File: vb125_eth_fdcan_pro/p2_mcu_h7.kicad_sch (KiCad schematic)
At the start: 14 parts, among them J1 TAGconnect NL, M1 DM-OLED042-647, U1 STM32H725IGKx

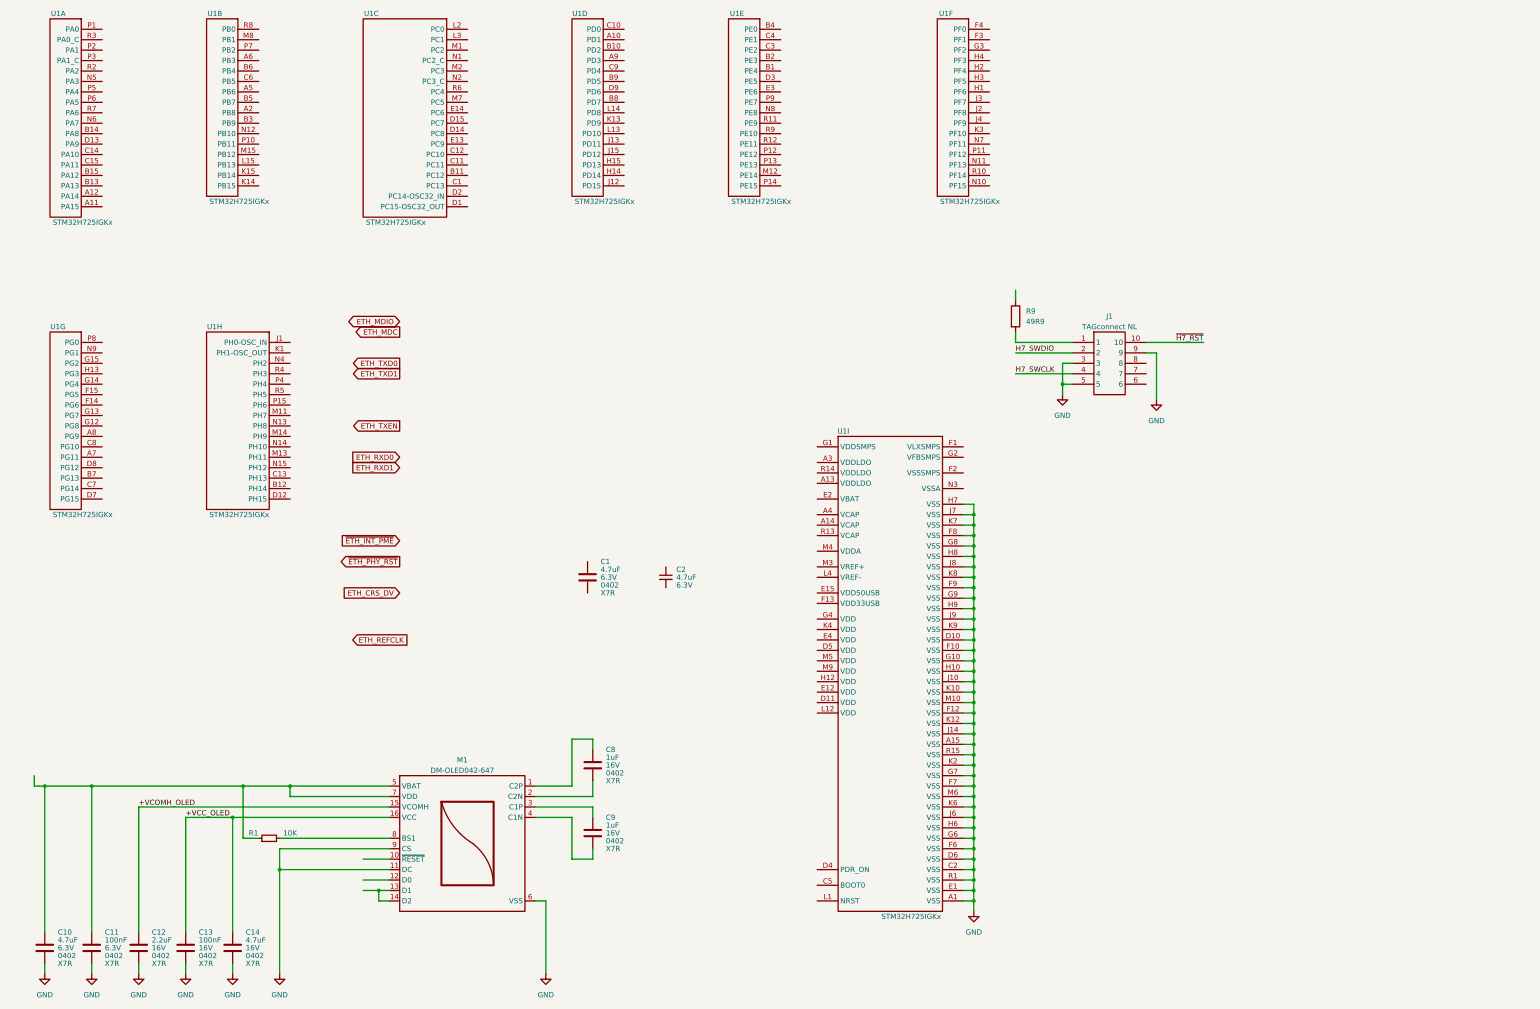
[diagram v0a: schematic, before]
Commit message: AOZ schematic. 3V3 DC-DC. Partly bus power.
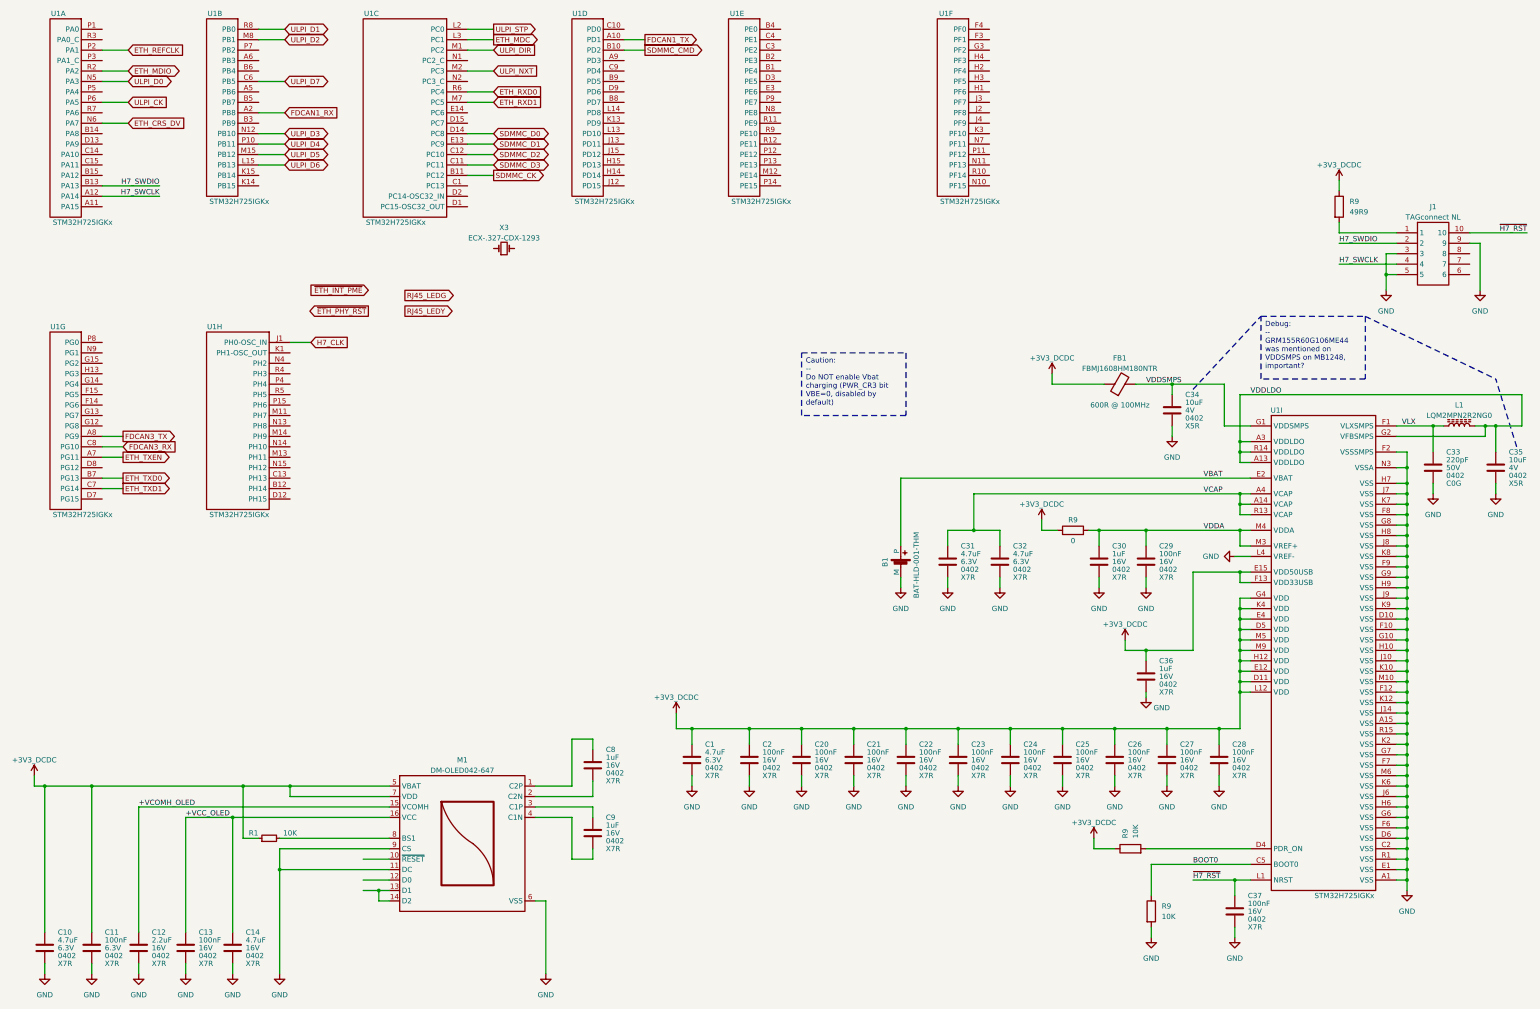
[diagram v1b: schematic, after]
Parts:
- removed C2: 4.7uF, symbol Device:C_Small
- added B1: BAT-HLD-001-THM, vhrd_connector_battery:BAT-HLD-001-THM, symbol vhrd_connector_battery:BAT-HLD-001-THM
- added C2, C20, C21, C22, C23, C24, C25, C26, C27, C28, C29, C37: 100nF, symbol Device:C
- added C30, C36: 1uF, symbol Device:C
- added C31, C32: 4.7uF, symbol Device:C
- added C33: 220pF, symbol Device:C
- added C34, C35: 10uF, symbol Device:C
- added FB1: FBMJ1608HM180NTR, symbol Device:FerriteBead
- added L1: LQM2MPN2R2NG0, symbol Device:L_Ferrite
- added R9 (x2): 10K, Resistor_SMD:R_0402_1005Metric, symbol Device:R
- added R9: 0, Resistor_SMD:R_0402_1005Metric, symbol Device:R
- added X3: ECX-.327-CDX-1293, vhrd_cristal:ECX-.327-CDX-1293, symbol vhrd_crystal:ECX-.327-CDX-1293
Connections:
- net ETH_CRS_DV: now also U1.N6 (PA7)
- net ETH_MDC: now also U1.L3 (PC1)
- net ETH_MDIO: now also U1.R2 (PA2)
- net ETH_REFCLK: now also U1.P2 (PA1)
- net ETH_RXD0: now also U1.R6 (PC4)
- net ETH_RXD1: now also U1.M7 (PC5)
- net ETH_TXD0: now also U1.B7 (PG13)
- net ETH_TXD1: now also U1.C7 (PG14)
- net ETH_TXEN: now also U1.A7 (PG11)
- net GND: now also C1.2, U1.F2 (VSSSMPS), U1.L4 (VREF-), U1.N3 (VSSA), B1.M, C2.2, C20.2, C21.2, C22.2, C23.2, C24.2, C25.2, C26.2, C27.2, C28.2, C29.2, C30.2, C31.2, C32.2, C33.2, C34.2, C35.2, C36.2, C37.2, R9.2
- net H7_SWCLK: now also U1.A12 (PA14)
- net H7_SWDIO: now also U1.B13 (PA13)
- net ~{H7_RST}: now also U1.L1 (NRST), C37.1
- net ULPI_D0: now reaches U1.N5 (PA3)
- net ULPI_CK: now reaches U1.P6 (PA5)
- net VDDLDO: now reaches U1.A13 (VDDLDO)
- net VDDLDO: now also U1.A3 (VDDLDO), U1.G2 (VFBSMPS), U1.R14 (VDDLDO), C35.1, L1.2
- net VCAP: now reaches U1.A14 (VCAP)
- net VCAP: now also U1.A4 (VCAP), U1.R13 (VCAP), C31.1, C32.1
- net BOOT0: now reaches U1.C5 (BOOT0)
- net BOOT0: now also R9.1
- net +3V3_DCDC: now reaches U1.D11 (VDD)
- net +3V3_DCDC: now also C1.1, C10.1, C11.1, M1.5 (VBAT), M1.7 (VDD), R1.1, R9.1, U1.D5 (VDD), U1.E12 (VDD), U1.E15 (VDD50USB), U1.E4 (VDD), U1.F13 (VDD33USB), U1.G4 (VDD), U1.H12 (VDD), U1.K4 (VDD), U1.L12 (VDD), U1.M5 (VDD), U1.M9 (VDD), C2.1, C20.1, C21.1, C22.1, C23.1, C24.1, C25.1, C26.1, C27.1, C28.1, C36.1, FB1.1, R9.1, R9.1
- net at U1.D4 (PDR_ON): now also R9.2
- net VBAT: now reaches U1.E2 (VBAT)
- net VBAT: now also B1.P
- net VLX: now reaches U1.F1 (VLXSMPS)
- net VLX: now also C33.1, L1.1
- net VDDSMPS: now reaches U1.G1 (VDDSMPS)
- net VDDSMPS: now also C34.1, FB1.2
- net VDDA: now reaches U1.M3 (VREF+)
- net VDDA: now also U1.M4 (VDDA), C29.1, C30.1, R9.2
- net H7_CLK: now reaches U1.J1 (PH0-OSC_IN)
- net FDCAN1_TX: now reaches U1.A10 (PD1)
- net SDMMC_CMD: now reaches U1.B10 (PD2)
- net FDCAN3_TX: now reaches U1.A8 (PG9)
- net FDCAN3_RX: now reaches U1.C8 (PG10)
- net SDMMC_CK: now reaches U1.B11 (PC12)
- net SDMMC_D3: now reaches U1.C11 (PC11)
- net SDMMC_D2: now reaches U1.C12 (PC10)
- net SDMMC_D0: now reaches U1.D14 (PC8)
- net SDMMC_D1: now reaches U1.E13 (PC9)
- net ULPI_STP: now reaches U1.L2 (PC0)
- net ULPI_DIR: now reaches U1.M1 (PC2)
- net ULPI_NXT: now reaches U1.M2 (PC3)
- net FDCAN1_RX: now reaches U1.A2 (PB8)
- net ULPI_D7: now reaches U1.C6 (PB5)
- net ULPI_D6: now reaches U1.L15 (PB13)
- net ULPI_D5: now reaches U1.M15 (PB12)
- net ULPI_D2: now reaches U1.M8 (PB1)
- net ULPI_D3: now reaches U1.N12 (PB10)
- net ULPI_D4: now reaches U1.P10 (PB11)
- net ULPI_D1: now reaches U1.R8 (PB0)
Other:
- moved on the sheet: C1, J1, R9, U1I

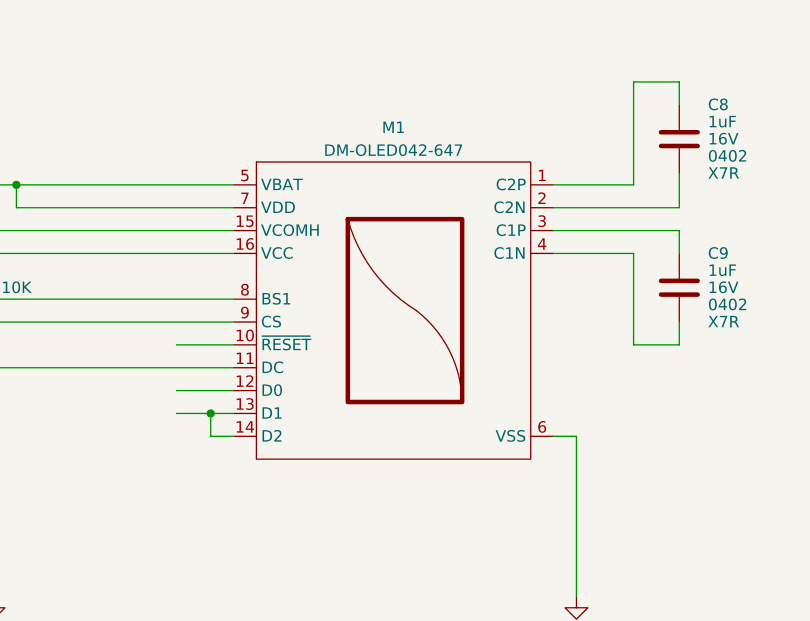
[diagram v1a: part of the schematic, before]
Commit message: Work on PoE. Rearrange pages.
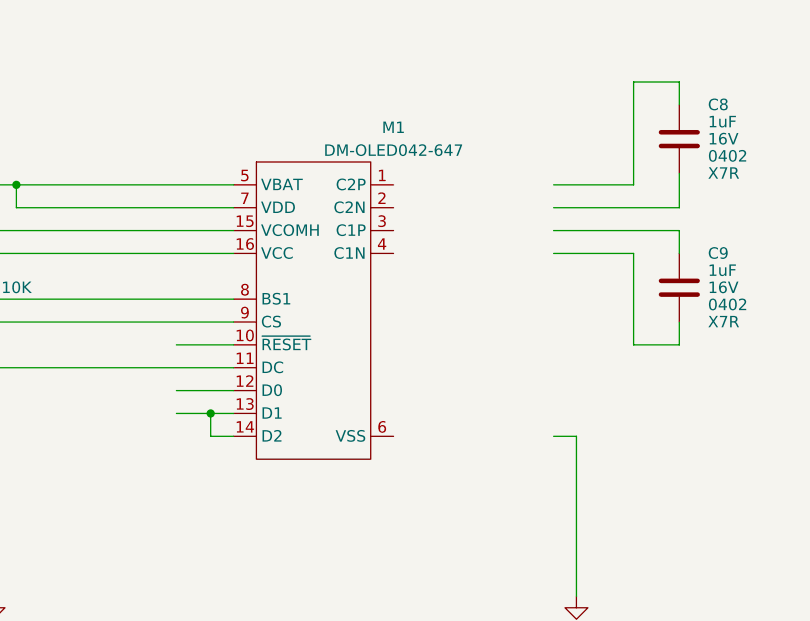
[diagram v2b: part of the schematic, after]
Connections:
- net GND: no longer M1.6 (VSS)
- net at C8.1: no longer M1.1 (C2P)
- net at C8.2: no longer M1.2 (C2N)
- net at C9.1: no longer M1.3 (C1P)
- net at C9.2: no longer M1.4 (C1N)
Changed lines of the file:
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@@
       (effects (font (size 1.27 1.27)) hide)
     )
-    (property "Datasheet" "https://cdn.shopify.com/s/files/1/0264/7629/files/DM-OLED042-647_Datasheet_172e9a12-376c-4f72-95bb-83c6a7033324.pdf?v=1675320439" (at 120.65 245.11 0)
+    (property "Datasheet" "https://drive.google.com/file/d/1ygmyopC3FinO5EHa4Gdgm3Pccdjo0d4R/view" (at 120.65 245.11 0)
       (effects (font (size 1.27 1.27)) hide)
     )

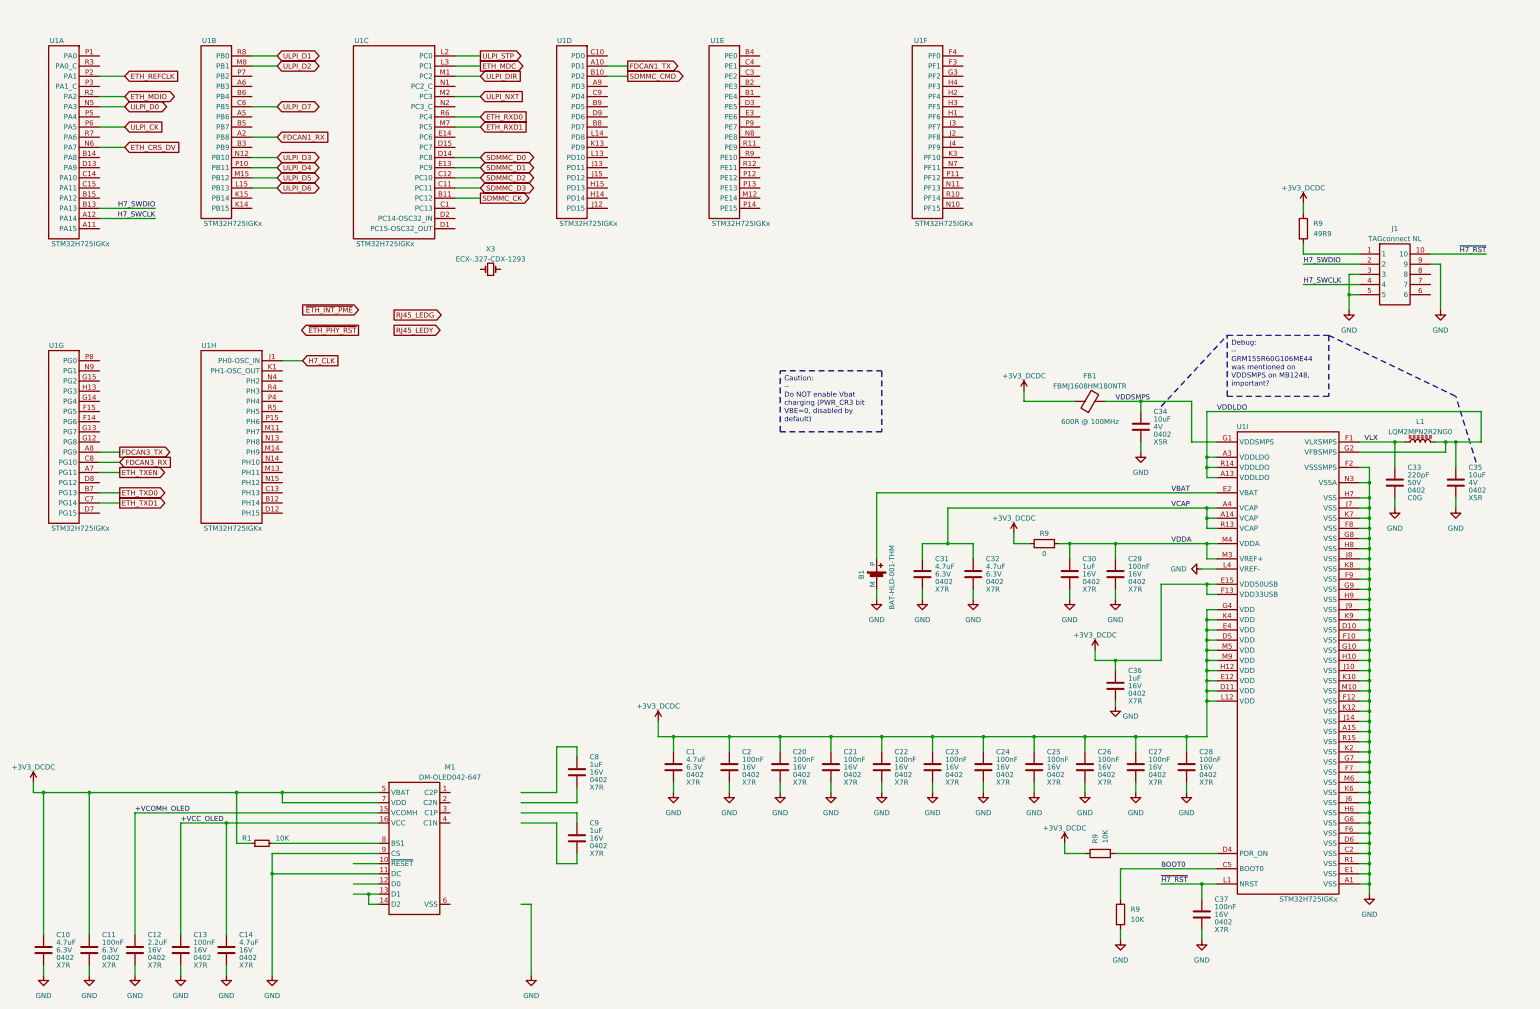
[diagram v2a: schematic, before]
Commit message: CAN schematics. Assign IO on H7.
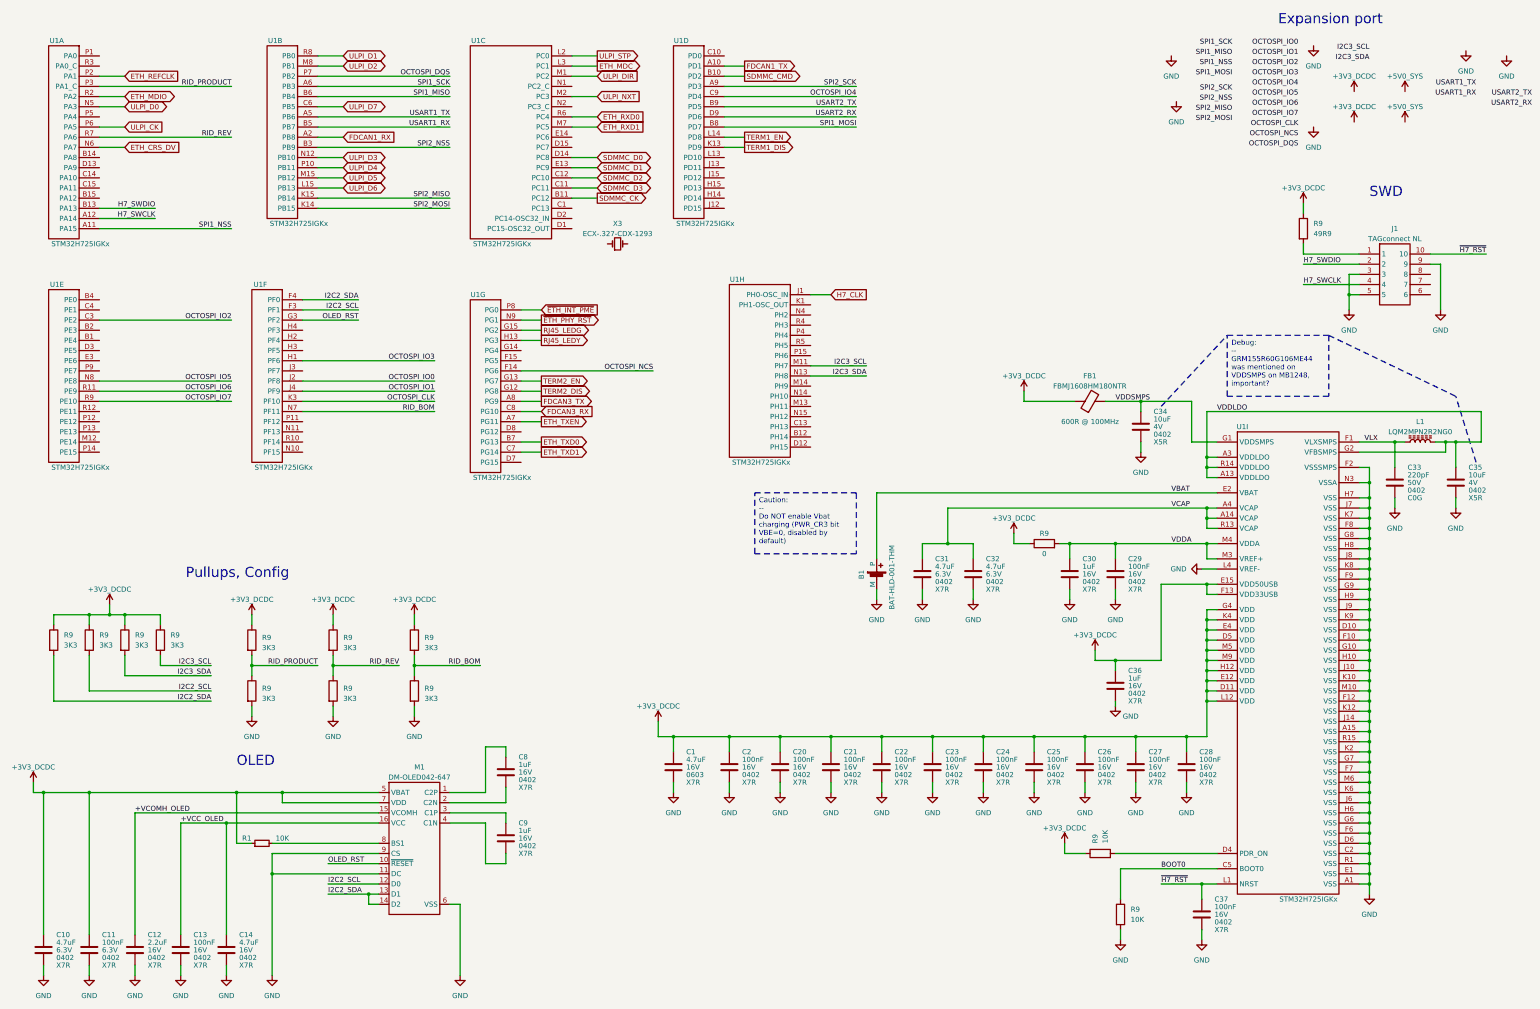
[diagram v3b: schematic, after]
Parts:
- added R9 (x10): 3K3, Resistor_SMD:R_0402_1005Metric, symbol Device:R
- C1: footprint (none) -> Capacitor_SMD:C_0603_1608Metric; Package 0402 -> 0603; Voltage 6.3V -> 16V; Vworking 3.3V -> 8.7V
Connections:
- net +3V3_DCDC: now also R9.1, R9.1, R9.1, R9.1, R9.1, R9.1, R9.1
- net GND: now also M1.6 (VSS), R9.2, R9.2, R9.2
- net RJ45_LEDG: now also U1.G15 (PG2)
- net RJ45_LEDY: now also U1.H13 (PG3)
- net ~{ETH_INT_PME}: now also U1.P8 (PG0)
- net ~{ETH_PHY_RST}: now also U1.N9 (PG1)
- net SPI1_NSS: now reaches U1.A11 (PA15)
- net RID_PRODUCT: now reaches U1.P3 (PA1_C)
- net RID_PRODUCT: now also R9.1, R9.2
- net RID_REV: now reaches U1.R7 (PA6)
- net RID_REV: now also R9.1, R9.2
- net I2C3_SCL: now reaches U1.M11 (PH7)
- net I2C3_SCL: now also R9.2
- net I2C3_SDA: now reaches U1.N13 (PH8)
- net I2C3_SDA: now also R9.2
- net at C8.1: now also M1.1 (C2P)
- net at C8.2: now also M1.2 (C2N)
- net SPI2_SCK: now reaches U1.A9 (PD3)
- net SPI1_MOSI: now reaches U1.B8 (PD7)
- net USART2_TX: now reaches U1.B9 (PD5)
- net OCTOSPI_IO4: now reaches U1.C9 (PD4)
- net USART2_RX: now reaches U1.D9 (PD6)
- net TERM1_DIS: now reaches U1.K13 (PD9)
- net TERM1_EN: now reaches U1.L14 (PD8)
- net I2C2_SCL: now reaches U1.F3 (PF1)
- net I2C2_SCL: now also M1.12 (D0), R9.2
- net I2C2_SDA: now reaches U1.F4 (PF0)
- net I2C2_SDA: now also M1.13 (D1), M1.14 (D2), R9.2
- net OLED_RST: now reaches U1.G3 (PF2)
- net OLED_RST: now also M1.10 (~{RESET})
- net OCTOSPI_IO3: now reaches U1.H1 (PF6)
- net OCTOSPI_IO0: now reaches U1.J2 (PF8)
- net OCTOSPI_IO1: now reaches U1.J4 (PF9)
- net OCTOSPI_CLK: now reaches U1.K3 (PF10)
- net RID_BOM: now reaches U1.N7 (PF11)
- net RID_BOM: now also R9.1, R9.2
- net OCTOSPI_NCS: now reaches U1.F14 (PG6)
- net TERM2_DIS: now reaches U1.G12 (PG8)
- net TERM2_EN: now reaches U1.G13 (PG7)
- net at C9.1: now also M1.3 (C1P)
- net at C9.2: now also M1.4 (C1N)
- net OCTOSPI_IO2: now reaches U1.C3 (PE2)
- net OCTOSPI_IO5: now reaches U1.N8 (PE8)
- net OCTOSPI_IO6: now reaches U1.R11 (PE9)
- net OCTOSPI_IO7: now reaches U1.R9 (PE10)
- net USART1_TX: now reaches U1.A5 (PB6)
- net SPI1_SCK: now reaches U1.A6 (PB3)
- net SPI2_NSS: now reaches U1.B3 (PB9)
- net USART1_RX: now reaches U1.B5 (PB7)
- net SPI1_MISO: now reaches U1.B6 (PB4)
- net SPI2_MOSI: now reaches U1.K14 (PB15)
- net SPI2_MISO: now reaches U1.K15 (PB14)
- net OCTOSPI_DQS: now reaches U1.P7 (PB2)
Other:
- note added: "Expansion port"
- note added: "OLED"
- note added: "Pullups, Config"
- note added: "SWD"
- moved on the sheet: C8, C9, U1B, U1C, U1D, U1E, U1F, U1G, U1H, X3
